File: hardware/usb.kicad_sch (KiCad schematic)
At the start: 6 parts, among them J601 USB_C_Receptacle_USB2.0, U601 SRV05-4

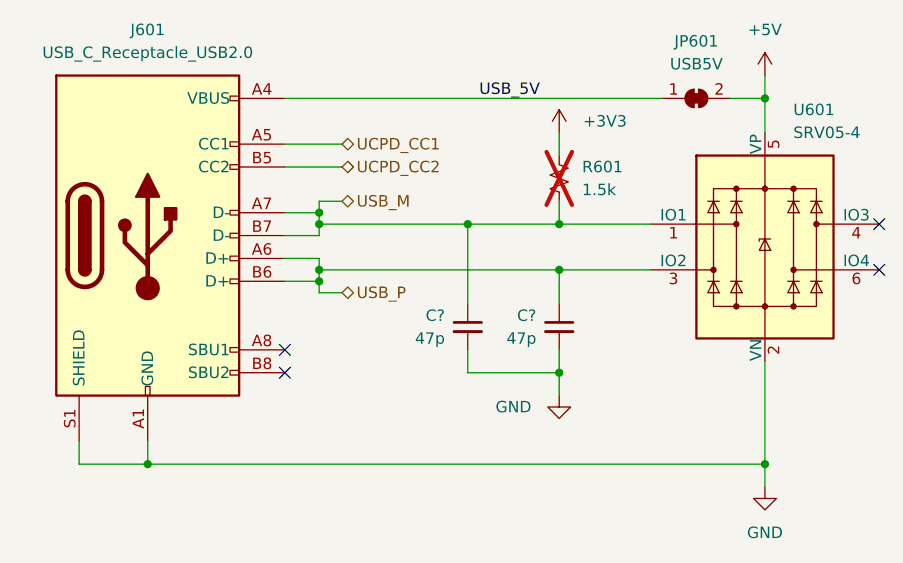
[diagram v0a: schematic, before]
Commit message: new hardware layout for IIS2ICLX
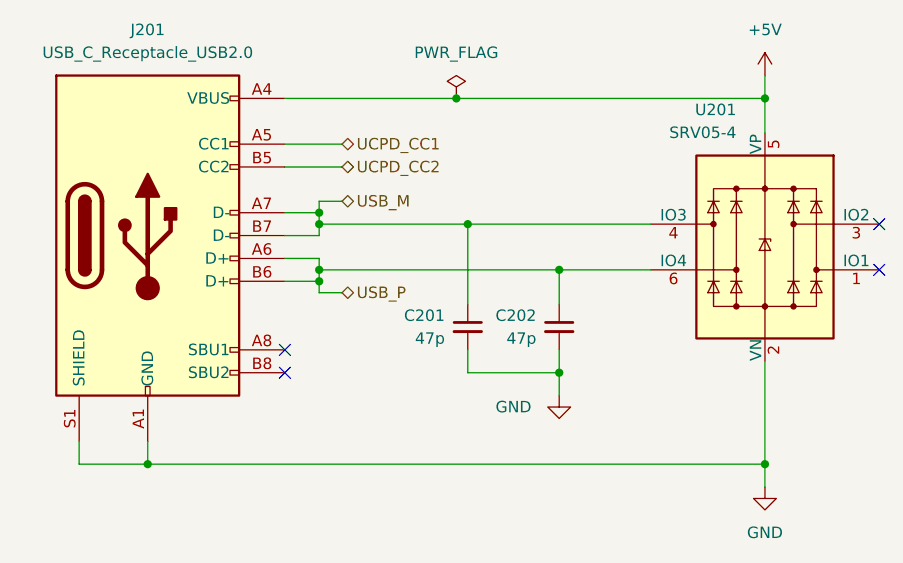
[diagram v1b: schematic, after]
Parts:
- removed JP601: USB5V, Jumper:SolderJumper-2_P1.3mm_Bridged_RoundedPad1.0x1.5mm, symbol Jumper:SolderJumper_2_Bridged
- removed R601: 1.5k, Resistor_SMD:R_0402_1005Metric, symbol Device:R_Small_US
- C201, C202: renamed from C?; LCSC ID (none) -> C1567
- J201: renamed from J601; symbol Connector:USB_C_Receptacle_USB2.0 -> Connector:USB_C_Receptacle_USB2.0_16P; LCSC ID (none) -> C165948
- U201: renamed from U601; LCSC ID (none) -> C7420376
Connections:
- net USB_5V is gone; now on net +5V: J201.A4 (VBUS), J201.A9 (VBUS), J201.B4 (VBUS), J201.B9 (VBUS)
- net USB_M: now also U201.4 (IO3); no longer U201.1 (IO1)
- net USB_P: now also U201.6 (IO4); no longer U201.3 (IO2)
